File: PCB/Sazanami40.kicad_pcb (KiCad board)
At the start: 2 copper layers, 84 parts, among them SW1 SW_PUSH, SW10 SW_PUSH, SW11 SW_PUSH, SW12 SW_PUSH, SW13 SW_PUSH, SW14 SW_PUSH, SW15 SW_PUSH, SW16 SW_PUSH, SW17 SW_PUSH, SW18 SW_PUSH, SW19 SW_PUSH, SW2 SW_PUSH, SW20 SW_PUSH, SW21 SW_PUSH, SW22 SW_PUSH, SW23 SW_PUSH, SW24 SW_PUSH, SW25 SW_PUSH, SW26 SW_PUSH, SW27 SW_PUSH, SW28 SW_PUSH, SW29 SW_PUSH, SW3 SW_PUSH, SW30 SW_PUSH, SW31 SW_PUSH, SW32 SW_PUSH, SW33 SW_PUSH, SW34 SW_PUSH, SW35 SW_PUSH, SW36 SW_PUSH, SW37 SW_PUSH, SW38 SW_PUSH, SW39 SW_PUSH, SW4 SW_PUSH, SW40 SW_PUSH, SW41 SW_PUSH, SW42 SW_PUSH, SW43 SW_PUSH, SW5 SW_PUSH, SW6 SW_PUSH, SW7 SW_PUSH, SW8 SW_PUSH, SW9 SW_PUSH, U1 ProMicro

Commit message: layout complete :
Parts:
- added D41: D, Diode_SMD:D_SOD-123, B.Cu at (328.7, 98.5)
- added D42: D, Diode_SMD:D_SOD-123, B.Cu at (340.8, 57.7)
- added SW44: SW_PUSH, Keebio-Parts:MX_PCB_100H, F.Cu at (347.4, 95.2)
- added SW45: SW_PUSH, kbd:ResetSW, F.Cu at (209.6, 110.7)
- D1, D10, D11, D12, D13, D14, D15, D16, D17, D18, D19, D2, D20, D21, D22, D23, D24, D25, D26, D27, D28, D29, D3, D30, D31, D32, D33, D34, D35, D36, D37, D38, D39, D4, D40, D5, D6, D7, D8, D9: moved to B.Cu
- SW1, SW10, SW11, SW12, SW13, SW14, SW15, SW16, SW17, SW18, SW19, SW2, SW20, SW21, SW22, SW23, SW24, SW25, SW26, SW27, SW28, SW29, SW3, SW30, SW31, SW32, SW33, SW34, SW35, SW36, SW37, SW38, SW39, SW4, SW40, SW41, SW42, SW5, SW6, SW7, SW8, SW9: footprint footprints:CHERRY_PCB_100H -> Keebio-Parts:MX_PCB_100H
- SW43: footprint kbd:ResetSW -> Keebio-Parts:MX_PCB_100H
- moved SW43 322.2 mm to (344.1, 76.5), turned to 10 degrees
- moved SW41 301.0 mm to (328.7, 98.5), turned to 10 degrees
- moved SW42 296.3 mm to (340.8, 57.7), turned to 10 degrees
- moved D40 295.5 mm to (325.4, 79.8), turned to 10 degrees
- moved D39 294.9 mm to (322.0, 61.0), turned to 10 degrees
- moved D37 286.2 mm to (304.9, 73.7), turned to 10 degrees
- moved D36 281.2 mm to (301.6, 54.9), turned to 10 degrees
- moved SW38 279.7 mm to (308.3, 92.5), turned to 10 degrees
- moved D38 277.9 mm to (308.3, 92.5), turned to 10 degrees
- moved SW39 275.2 mm to (322.0, 61.0), turned to 10 degrees
- moved SW40 265.9 mm to (325.4, 79.8), turned to 10 degrees
- moved D35 265.8 mm to (292.0, 109.8), turned to 10 degrees
- moved D32 261.8 mm to (282.0, 53.6), turned to 10 degrees
- moved D34 258.6 mm to (288.7, 91.1), turned to 10 degrees
- moved SW36 254.3 mm to (301.6, 54.9), turned to 10 degrees
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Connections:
- D13 pad 1: row0 -> row3
- D13 pad 2: Net-(D13-Pad2) -> row2
- D14 pad 1: row1 -> row0
- D15 pad 1: row2 -> row1
- D16 pad 1: row3 -> row2
- D17 pad 1: row0 -> row3
- D18 pad 1: row1 -> row0
- D19 pad 1: row2 -> row1
- D20 pad 1: row3 -> row2
- D21 pad 1: row0 -> row3
- D22 pad 1: row1 -> row0
- D23 pad 1: row2 -> row1
- D24 pad 1: row3 -> row2
- D25 pad 1: row0 -> row3
- D26 pad 1: row1 -> row0
- D27 pad 1: row2 -> row1
- D28 pad 1: row3 -> row2
- D29 pad 1: row0 -> row3
- D30 pad 1: row1 -> row0
- D31 pad 1: row2 -> row1
- D32 pad 1: row0 -> row2
- D33 pad 1: row1 -> row3
- D33 pad 2: Net-(D33-Pad2) -> row2
- D34 pad 1: row2 -> row0
- D35 pad 1: row0 -> row1
- D36 pad 1: row1 -> row2
- D37 pad 1: row2 -> row0
- D38 pad 1: row0 -> row1
- D39 pad 1: row1 -> row2
- D40 pad 1: row2 -> row0
- SW13 pad 1: col4 -> col3
- SW13 pad 2: Net-(D13-Pad2) -> row2
- SW17 pad 1: col5 -> col4
- SW21 pad 2: Net-(D20-Pad2) -> Net-(D21-Pad2)
- SW22 pad 1: col6 -> col5
- SW26 pad 2: Net-(D24-Pad2) -> Net-(D25-Pad2)
- SW27 pad 1: col7 -> col6
- SW31 pad 1: col8 -> col7
- SW34 pad 1: col9 -> col8
- SW35 pad 1: col9 -> col8
- SW35 pad 2: Net-(D33-Pad2) -> row2
- SW37 pad 1: col10 -> col9
- SW38 pad 1: col10 -> col9
- SW40 pad 1: col11 -> col10
- SW41 pad 1: col11 -> col10
- SW43 pad 1: reset -> col11
- SW43 pad 2: +5V -> Net-(D41-Pad2)
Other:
- rule pad_to_mask_clearance: 0.051 -> 0

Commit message: first draft PCB complete
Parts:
- moved D22 107.0 mm to (255.0, 71.5), turned to 100 degrees
- moved SW18 57.9 mm to (172.9, 69.8)
- moved D26 54.9 mm to (257.5, 71.0), turned to 100 degrees
- moved D18 53.9 mm to (164.0, 71.5), turned to 80 degrees
- moved D31 53.6 mm to (294.0, 72.5), turned to 100 degrees
- moved D30 51.6 mm to (291.0, 56.0), turned to 100 degrees
- moved SW45 44.9 mm to (192.9, 69.1), turned to 270 degrees
- moved D39 42.4 mm to (337.5, 100.5), turned to 100 degrees
- moved D42 42.3 mm to (340.0, 100.0), turned to 100 degrees
- moved D28 42.3 mm to (264.0, 108.5), turned to 100 degrees
- moved D33 42.0 mm to (300.5, 111.5), turned to 100 degrees
- moved D32 41.9 mm to (297.5, 92.5), turned to 100 degrees
- moved D35 38.1 mm to (296.5, 72.0), turned to 100 degrees
- moved D36 37.1 mm to (300.0, 92.0), turned to 100 degrees
- moved D34 35.9 mm to (293.5, 55.5), turned to 100 degrees
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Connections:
- net +5V renamed GND
- D13 pad 2: row2 -> Net-(D13-Pad2)
- D33 pad 2: row2 -> Net-(D33-Pad2)
- SW13 pad 2: row2 -> Net-(D13-Pad2)
- SW35 pad 2: row2 -> Net-(D33-Pad2)
- U1 pad 10: Net-(U1-Pad10) -> col6
- U1 pad 11: Net-(U1-Pad11) -> row3
- U1 pad 12: Net-(U1-Pad12) -> row2
- U1 pad 13: Net-(U1-Pad13) -> col0
- U1 pad 14: Net-(U1-Pad14) -> col1
- U1 pad 15: Net-(U1-Pad15) -> col2
- U1 pad 16: Net-(U1-Pad16) -> col3
- U1 pad 17: Net-(U1-Pad17) -> col4
- U1 pad 18: Net-(U1-Pad18) -> col5
- U1 pad 19: Net-(U1-Pad19) -> row1
- U1 pad 20: Net-(U1-Pad20) -> row0
- U1 pad 5: Net-(U1-Pad5) -> col11
- U1 pad 6: Net-(U1-Pad6) -> col10
- U1 pad 7: Net-(U1-Pad7) -> col9
- U1 pad 8: Net-(U1-Pad8) -> col8
- U1 pad 9: Net-(U1-Pad9) -> col7
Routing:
- net row2: track 0.00 -> 368.5 mm, vias 0 -> 1
- net row3: track 0.00 -> 314.8 mm
- net row1: track 0.00 -> 303.8 mm, vias 0 -> 2
- net row0: track 0.00 -> 295.7 mm
- net col0: track 0.00 -> 242.5 mm
- net col1: track 0.00 -> 224.8 mm
- net col2: track 0.00 -> 215.2 mm
- net col3: track 0.00 -> 205.5 mm
- net col11: track 0.00 -> 203.4 mm
- net col4: track 0.00 -> 193.9 mm
- net col10: track 0.00 -> 189.4 mm
- net col5: track 0.00 -> 175.5 mm
- net col8: track 0.00 -> 165.8 mm
- net col9: track 0.00 -> 164.2 mm
- net col7: track 0.00 -> 137.7 mm
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- added copper zone on B.Cu, net GND
- added copper zone on F.Cu, net GND
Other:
- board outline added: 319.1 x 111.9 mm

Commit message: pcb complete
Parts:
- added G***: LOGO, emptystring:sazanamiLogo, B.Cu at (209.6, 107.2)
- added G***: LOGO, emptystring:sazanamiKanji, F.Cu at (209.6, 107.2)
- added Ref**: Val**, kbd:HOLE, F.Cu at (181.0, 121.4)
- added Ref**: Val**, kbd:HOLE, F.Cu at (166.7, 52.4)
- added Ref**: Val**, kbd:HOLE, F.Cu at (252.4, 52.4)
- added Ref**: Val**, kbd:HOLE, F.Cu at (331.0, 45.2)
- added Ref**: Val**, kbd:HOLE, F.Cu at (88.1, 45.2)
- added Ref**: Val**, kbd:HOLE, F.Cu at (88.1, 111.9)
- added Ref**: Val**, kbd:HOLE, F.Cu at (331.0, 111.9)
- added Ref**: Val**, kbd:HOLE, F.Cu at (238.1, 121.4)
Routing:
- net col7: track 137.7 -> 149.6 mm
- net col6: track 133.1 -> 122.0 mm
- net col10: track 189.4 -> 193.5 mm
- net col9: track 164.2 -> 167.9 mm
- net col8: track 165.8 -> 168.8 mm
- net row0: track 295.7 -> 293.6 mm
- net col11: track 203.4 -> 205.3 mm
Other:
- outline, holes or cut-outs redrawn
- board text added: "Sazanami40 by emptystring @SA_EndlessGame"

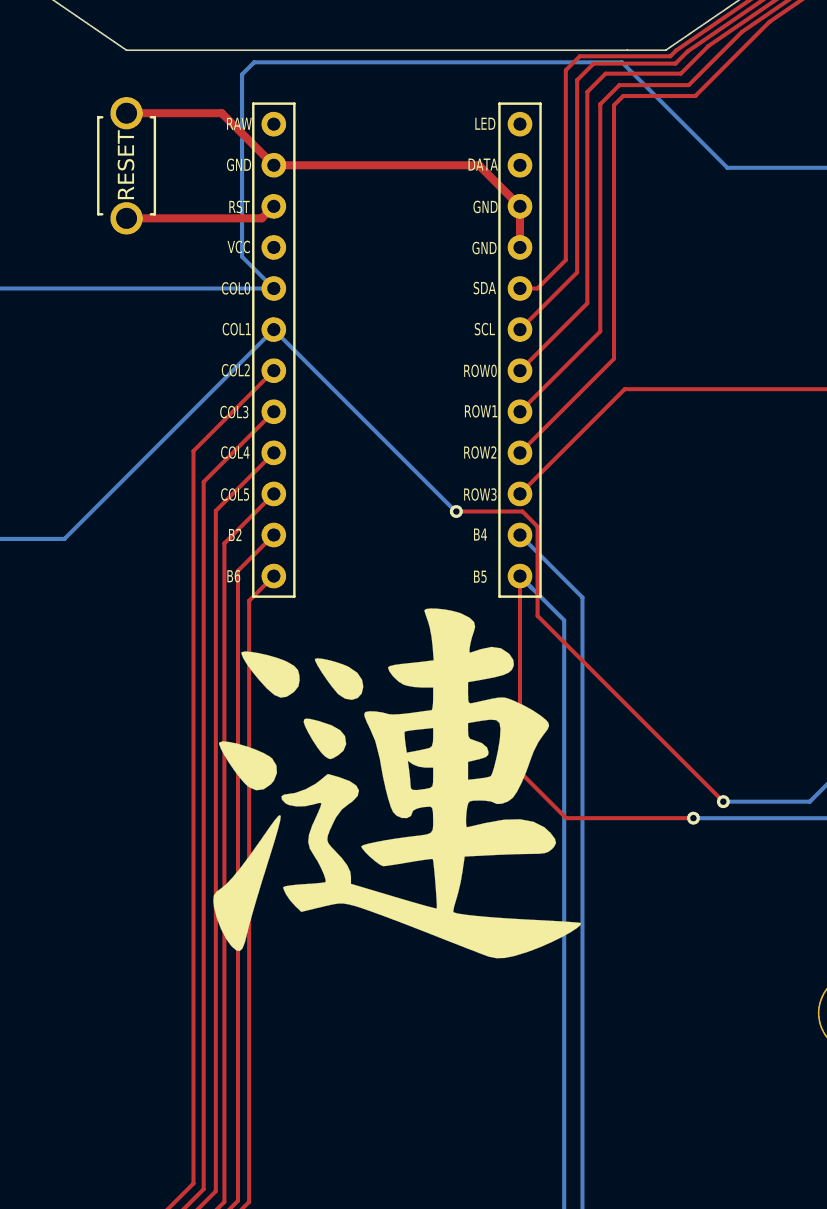
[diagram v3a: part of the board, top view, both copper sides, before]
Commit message: fixed reset switch position
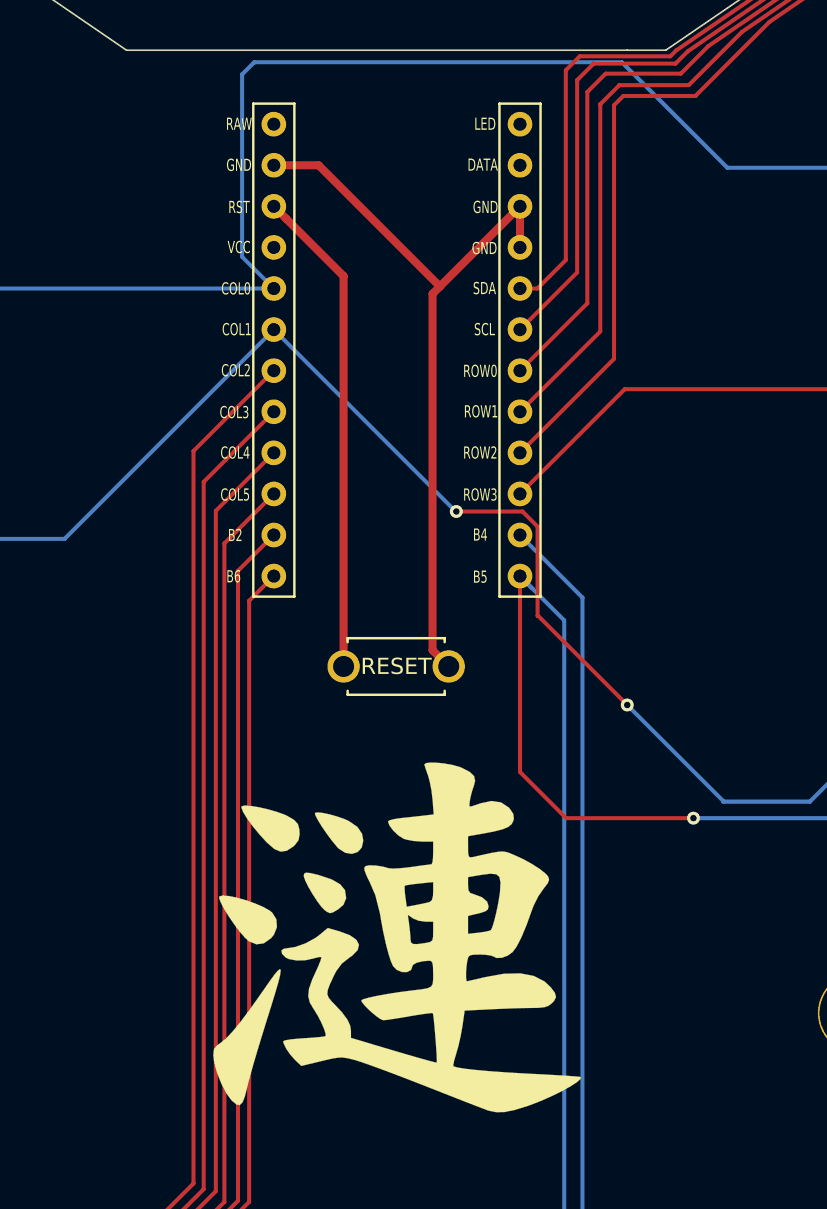
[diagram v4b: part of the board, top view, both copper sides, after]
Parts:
- moved SW45 35.2 mm to (209.6, 100.0), turned to 180 degrees
- moved G*** 9.53 mm to (209.6, 116.7) (x2)
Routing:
- net reset: track 9.41 -> 30.2 mm
- net GND: track 29.3 -> 47.0 mm
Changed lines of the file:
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@@
-(kicad_pcb (version 20171130) (host pcbnew "(5.0.1-3-g963ef8bb5)")
+(kicad_pcb (version 20171130) (host pcbnew "(5.1.0-0)")
   (general
     (thickness 1.6)
     (drawings 15)
-    (tracks 464)
+    (tracks 470)
     (zones 0)
     (modules 98)
@@
   )
   (setup
-    (last_trace_width 0.25)
+    (last_trace_width 0.5)
     (user_trace_width 0.5)
     (trace_clearance 0.2)
@@
     (zone_45_only no)
     (trace_min 0.2)
-    (segment_width 0.2)
-    (edge_width 0.1)
     (via_size 0.8)
     (via_drill 0.4)
@@
     (uvia_min_size 0.2)
     (uvia_min_drill 0.1)
+    (edge_width 0.1)
+    (segment_width 0.2)
     (pcb_text_width 0.3)
     (pcb_text_size 1.5 1.5)
@@
   )
   (module kbd:ResetSW (layer F.Cu)
-    (at 192.88125 69.05625 270)
-    (fp_text reference SW45 (at 0 2.55 270) (layer F.SilkS) hide
+    (at 209.55 100.0125 180)
+    (fp_text reference SW45 (at 0 2.55 180) (layer F.SilkS) hide
       (effects (font (size 1 1) (thickness 0.15)))
     )
-    (fp_text value SW_PUSH (at 0 -2.55 270) (layer F.Fab)
+    (fp_text value SW_PUSH (at 0 -2.55 180) (layer F.Fab)
       (effects (font (size 1 1) (thickness 0.15)))
     )
-    (fp_text user RESET (at 0.127 0 270) (layer B.SilkS)
+    (fp_text user RESET (at 0.127 0 180) (layer B.SilkS)
       (effects (font (size 1 1) (thickness 0.15)) (justify mirror))
     )
@@
     (fp_line (start -3 -1.75) (end 3 -1.75) (layer F.SilkS) (width 0.15))
     (fp_line (start 3 -1.75) (end 3 -1.5) (layer F.SilkS) (width 0.15))
-    (fp_text user RESET (at 0 0 270) (layer F.SilkS)
+    (fp_text user RESET (at 0 0 180) (layer F.SilkS)
       (effects (font (size 1 1) (thickness 0.15)))
     )
-    (pad 1 thru_hole circle (at 3.25 0 270) (size 2 2) (drill 1.3) (layers *.Cu *.Mask F.SilkS)
+    (pad 1 thru_hole circle (at 3.25 0 180) (size 2 2) (drill 1.3) (layers *.Cu *.Mask F.SilkS)
       (net 57 reset))
-    (pad 2 thru_hole circle (at -3.25 0 270) (size 2 2) (drill 1.3) (layers *.Cu *.Mask F.SilkS)
+    (pad 2 thru_hole circle (at -3.25 0 180) (size 2 2) (drill 1.3) (layers *.Cu *.Mask F.SilkS)
       (net 62 GND))
   )
@@
   )
   (module emptystring:sazanamiLogo (layer B.Cu)
-    (at 209.55 107.15625 180)
+    (at 209.55 116.68125 180)
     (fp_text reference G*** (at 0 0 180) (layer B.SilkS) hide
       (effects (font (size 1.524 1.524) (thickness 0.3)) (justify mirror))
@@
   )
   (module emptystring:sazanamiKanji (layer F.Cu)
-    (at 209.55 107.15625)
+    (at 209.55 116.68125)
     (fp_text reference G*** (at 0 0) (layer F.SilkS) hide
       (effects (font (size 1.524 1.524) (thickness 0.3)))
@@
   (segment (start 294.286519 74.124933) (end 276.786519 91.624933) (width 0.25) (layer B.Cu) (net 3) (status 10))
   (segment (start 160.713481 92.124933) (end 189.045967 92.124933) (width 0.25) (layer B.Cu) (net 3) (status 10))
-  (via (at 229.78 108.37) (size 0.8) (drill 0.4) (layers F.Cu B.Cu) (net 3))
   (segment (start 235.13 108.37) (end 229.78 108.37) (width 0.25) (layer B.Cu) (net 3))
   (segment (start 251.375067 92.124933) (end 235.13 108.37) (width 0.25) (layer B.Cu) (net 3))
   (segment (start 258.286519 92.124933) (end 251.375067 92.124933) (width 0.25) (layer B.Cu) (net 3) (status 10))
   (segment (start 189.045967 92.124933) (end 201.9864 79.1845) (width 0.25) (layer B.Cu) (net 3) (status 20))
-  (segment (start 229.78 108.37) (end 218.293401 96.883401) (width 0.25) (layer F.Cu) (net 3))
   (segment (start 218.293401 96.883401) (end 218.293401 91.362739) (width 0.25) (layer F.Cu) (net 3))
   (segment (start 218.293401 91.362739) (end 217.362163 90.431501) (width 0.25) (layer F.Cu) (net 3))
@@
   (via (at 213.27 90.431501) (size 0.8) (drill 0.4) (layers F.Cu B.Cu) (net 3))
   (segment (start 213.233401 90.431501) (end 201.9864 79.1845) (width 0.25) (layer B.Cu) (net 3) (status 20))
+  (via (at 223.8375 102.39375) (size 0.8) (drill 0.4) (layers F.Cu B.Cu) (net 3))
+  (segment (start 229.78 108.33625) (end 223.8375 102.39375) (width 0.25) (layer B.Cu) (net 3))
+  (segment (start 229.78 108.37) (end 229.78 108.33625) (width 0.25) (layer B.Cu) (net 3))
+  (segment (start 218.327151 96.883401) (end 218.293401 96.883401) (width 0.25) (layer F.Cu) (net 3))
+  (segment (start 223.8375 102.39375) (end 218.327151 96.883401) (width 0.25) (layer F.Cu) (net 3))
   (segment (start 82.786519 78.571646) (end 82.786519 79.875067) (width 0.25) (layer B.Cu) (net 4) (status 20))
   (segment (start 77.734055 73.519182) (end 82.786519 78.571646) (width 0.25) (layer B.Cu) (net 4))
@@
   (segment (start 218.28403 76.6445) (end 220.04 74.88853) (width 0.25) (layer F.Cu) (net 56))
   (segment (start 217.2064 76.6445) (end 218.28403 76.6445) (width 0.25) (layer F.Cu) (net 56))
-  (segment (start 192.88125 72.30625) (end 201.24465 72.30625) (width 0.5) (layer F.Cu) (net 57) (status 10))
-  (segment (start 201.24465 72.30625) (end 201.9864 71.5645) (width 0.5) (layer F.Cu) (net 57) (status 20))
-  (segment (start 192.88125 65.80625) (end 198.76815 65.80625) (width 0.5) (layer F.Cu) (net 62) (status 10))
-  (segment (start 198.76815 65.80625) (end 201.9864 69.0245) (width 0.5) (layer F.Cu) (net 62) (status 20))
-  (segment (start 201.9864 69.0245) (end 214.6664 69.0245) (width 0.5) (layer F.Cu) (net 62) (status 10))
-  (segment (start 214.6664 69.0245) (end 217.2064 71.5645) (width 0.5) (layer F.Cu) (net 62) (status 20))
+  (segment (start 202.748399 72.326499) (end 201.9864 71.5645) (width 0.5) (layer F.Cu) (net 57))
+  (segment (start 206.3 75.8781) (end 202.748399 72.326499) (width 0.5) (layer F.Cu) (net 57))
+  (segment (start 206.3 100.0125) (end 206.3 75.8781) (width 0.5) (layer F.Cu) (net 57))
   (segment (start 217.2064 71.5645) (end 217.2064 74.1045) (width 0.5) (layer F.Cu) (net 62) (status 30))
+  (segment (start 211.800001 99.012501) (end 212.8 100.0125) (width 0.5) (layer F.Cu) (net 62))
+  (segment (start 211.800001 76.970899) (end 211.800001 99.012501) (width 0.5) (layer F.Cu) (net 62))
+  (segment (start 201.9864 69.0245) (end 204.75575 69.0245) (width 0.5) (layer F.Cu) (net 62))
+  (segment (start 212.251075 76.519825) (end 211.800001 76.970899) (width 0.5) (layer F.Cu) (net 62))
+  (segment (start 204.75575 69.0245) (end 212.251075 76.519825) (width 0.5) (layer F.Cu) (net 62))
+  (segment (start 217.2064 71.5645) (end 212.251075 76.519825) (width 0.5) (layer F.Cu) (net 62))
   (segment (start 119.805362 106.89391) (end 119.286519 106.375067) (width 0.25) (layer B.Cu) (net 63) (status 20))
   (segment (start 123.799089 106.89391) (end 119.805362 106.89391) (width 0.25) (layer B.Cu) (net 63) (status 10))

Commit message: new logo front
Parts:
- removed the G*** at (209.6, 116.7)
- added G***: LOGO, emptystring:sazanamiHanko, F.Cu at (209.8, 116.7)
